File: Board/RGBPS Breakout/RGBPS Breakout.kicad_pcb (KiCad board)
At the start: 2 copper layers, 10 parts, among them J1 Conn_01x04_Pin, J2 Conn_01x01_Pin

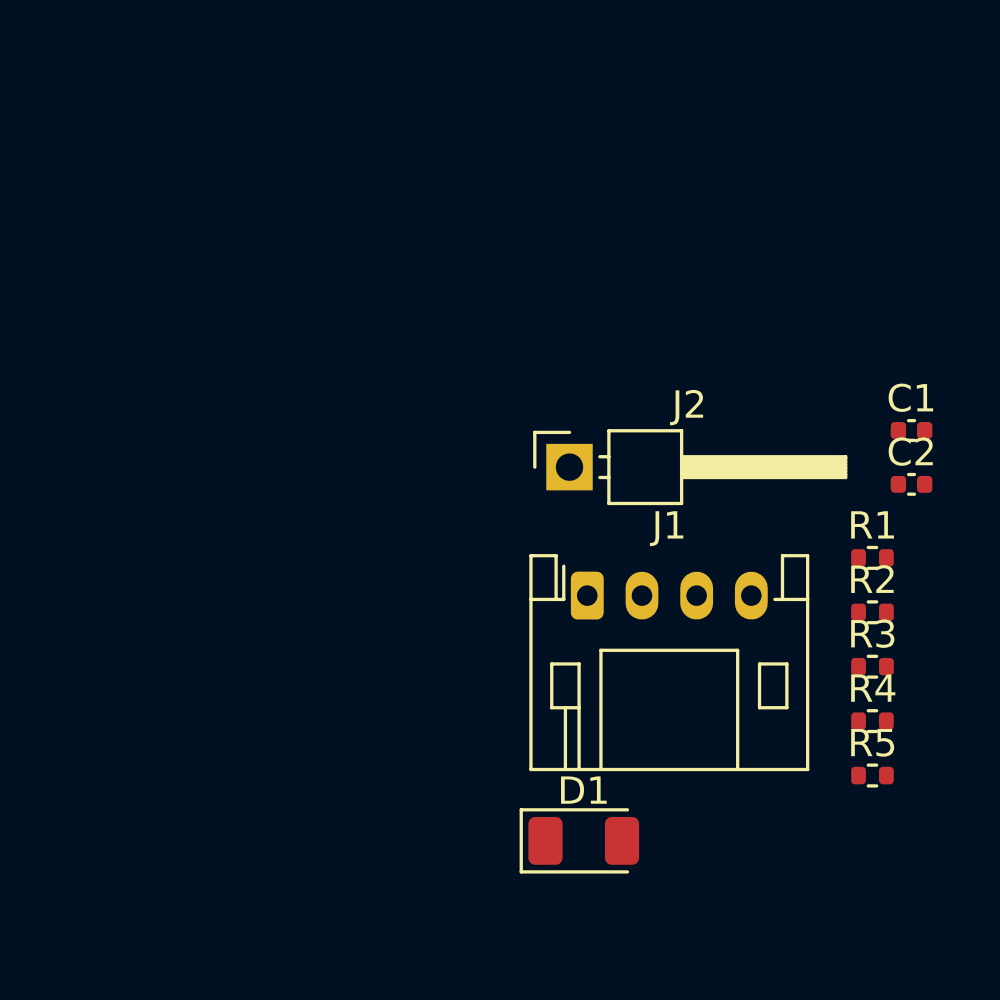
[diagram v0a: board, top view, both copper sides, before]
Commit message: bruuh footprint file is broken
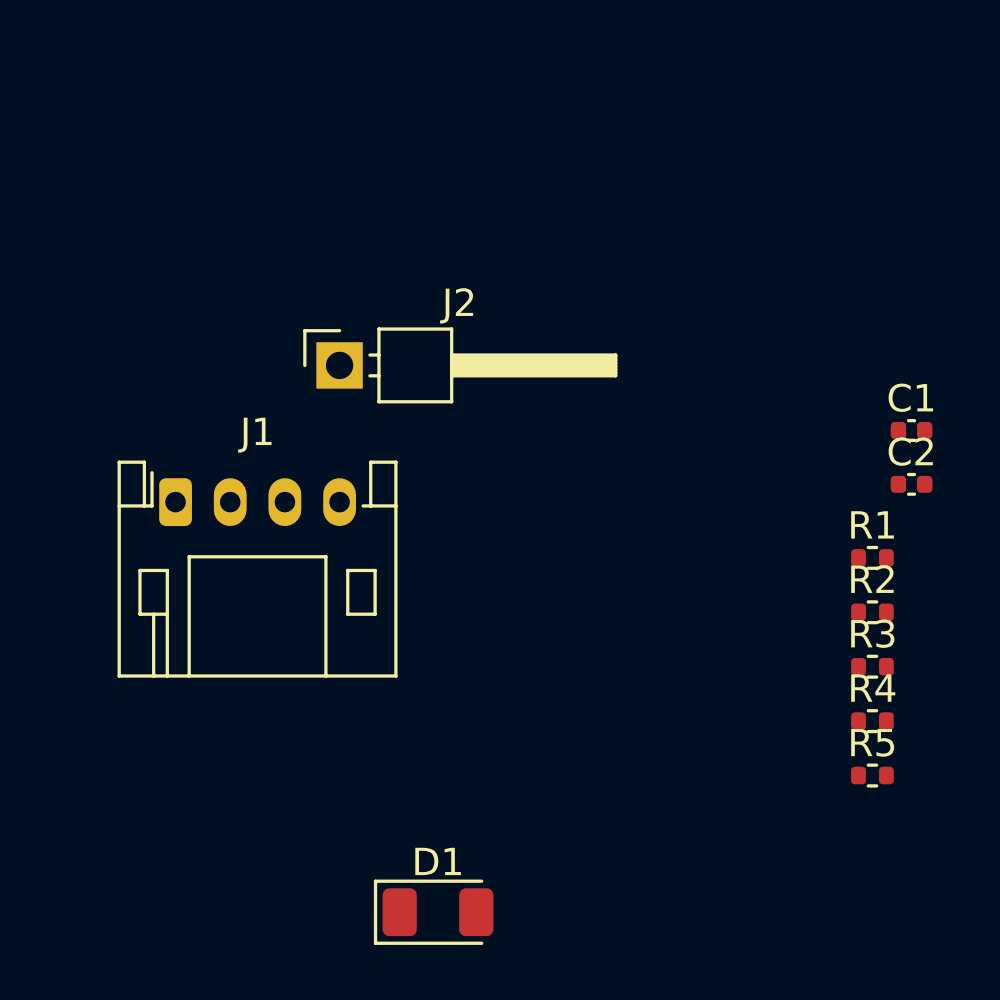
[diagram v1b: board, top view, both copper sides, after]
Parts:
- moved J1 15.4 mm to (129.0, 95.0)
- moved J2 9.20 mm to (135.0, 90.0)
- moved D1 5.93 mm to (138.6, 110.0)
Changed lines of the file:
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@@
 	(footprint "LED_SMD:LED_1206_3216Metric"
 		(layer "F.Cu")
-		(at 143.93 107.39)
+		(at 138.6 110)
 		(descr "LED SMD 1206 (3216 Metric), square (rectangular) end terminal, IPC_7351 nominal, (Body size source: http://www.tortai-tech.com/upload/download/2011102023233369053.pdf), generated with kicad-footprint-generator")
 		(tags "LED")
@@
 	(footprint "Connector_JST:JST_PH_S4B-PH-K_1x04_P2.00mm_Horizontal"
 		(layer "F.Cu")
-		(at 144.06 98.42)
+		(at 129 95)
 		(descr "JST PH series connector, S4B-PH-K (http://www.jst-mfg.com/product/pdf/eng/ePH.pdf), generated with kicad-footprint-generator")
 		(tags "connector JST PH top entry")
@@
 	(footprint "Connector_PinHeader_2.54mm:PinHeader_1x01_P2.54mm_Horizontal"
 		(layer "F.Cu")
-		(at 143.41 93.72)
+		(at 135 90)
 		(descr "Through hole angled pin header, 1x01, 2.54mm pitch, 6mm pin length, single row")
 		(tags "Through hole angled pin header THT 1x01 2.54mm single row")

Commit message: start routing, add zone fill for ground
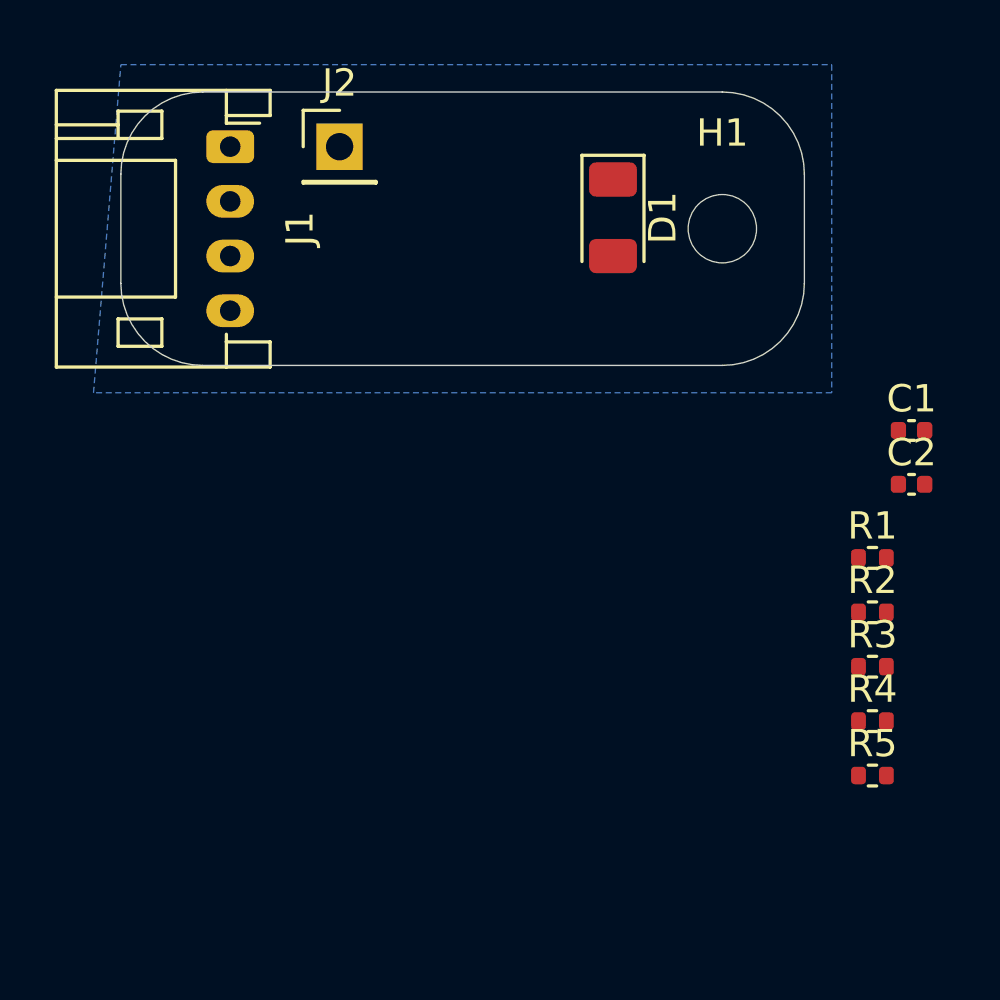
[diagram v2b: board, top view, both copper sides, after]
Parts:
- added H1: MountingHole, MountingHole:MountingHole_2.5mm, F.Cu at (149.0, 85.0)
- J2: footprint Connector_PinHeader_2.54mm:PinHeader_1x01_P2.54mm_Horizontal -> Connector_PinHeader_2.54mm:PinHeader_1x01_P2.54mm_Vertical
- moved D1 26.2 mm to (145.0, 84.6), turned to -90 degrees
- moved J1 13.2 mm to (131.0, 82.0), turned to -90 degrees
- moved J2 8.00 mm to (135.0, 82.0)
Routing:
- added copper zone on B.Cu, net GND
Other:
- board outline added: 25 x 10 mm

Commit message: routing
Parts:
- added IC1: APDS-9999, APDS-9999:APDS9999, F.Cu at (140.0, 85.5)
- D1: value 3.2V WHITE -> 2.8V WHITE
- R1: value 1.667 -> 7.7
- moved R3 24.5 mm to (137.8, 83.1), turned to 180 degrees
- moved R5 22.0 mm to (140.5, 88.0)
- moved R4 21.9 mm to (138.5, 88.0), turned to 180 degrees
- moved C2 19.1 mm to (140.9, 82.6), turned to -90 degrees
- moved R2 16.2 mm to (143.1, 87.5), turned to -90 degrees
- moved C1 14.5 mm to (143.1, 85.5), turned to 90 degrees
- moved R1 13.4 mm to (145.1, 87.5), turned to 180 degrees
- moved J2 0.70 mm to (134.9, 82.7)
- moved H1 0.23 mm to (149.2, 85.0)
- turned D1 to 90 degrees
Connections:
- D1 pad 1: +3.3V -> Net-(D1-K)
- D1 pad 2: Net-(D1-A) -> +3.3V
- R1 pad 1: Net-(D1-A) -> Net-(D1-K)
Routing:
- net +3.3V: track 0.00 -> 38.5 mm
- net SDA: track 0.00 -> 11.4 mm
- net SCL: track 0.00 -> 10.9 mm
- net INT: track 0.00 -> 7.25 mm
- net GND: track 0.00 -> 6.68 mm, vias 0 -> 3
- net Net-(IC1-VDD): track 0.00 -> 3.24 mm
- net Net-(D1-K): track 0.00 -> 1.77 mm
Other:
- board size 25 x 10 mm -> 25.4 x 10.4 mm
- board text added: "3V3"
- board text added: "GND"
- board text added: "I2C"
- board text added: "INT"
- board text added: "SCL"
- board text added: "SDA"
